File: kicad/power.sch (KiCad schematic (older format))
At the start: 12 parts, among them J4 UE27AC54100, U3 P-FET, U4 LM3671MF-3.3

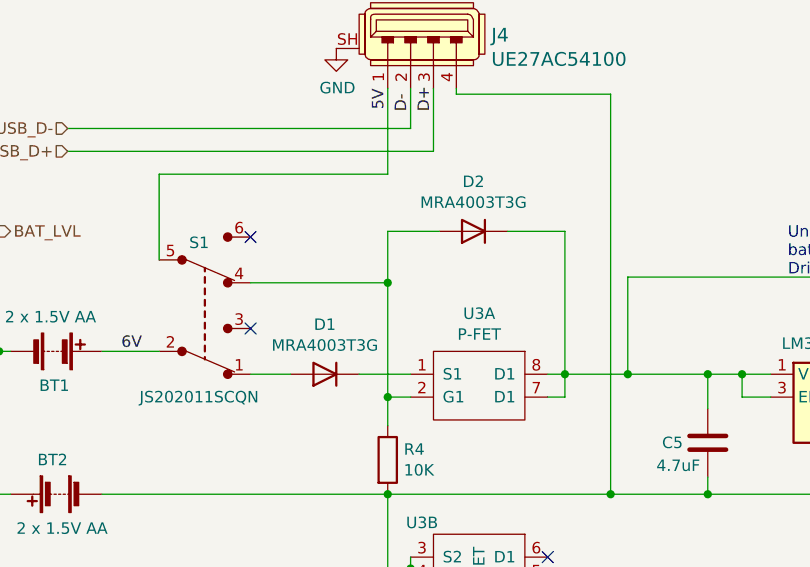
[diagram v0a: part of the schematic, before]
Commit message: Wired up buzzer and LDR
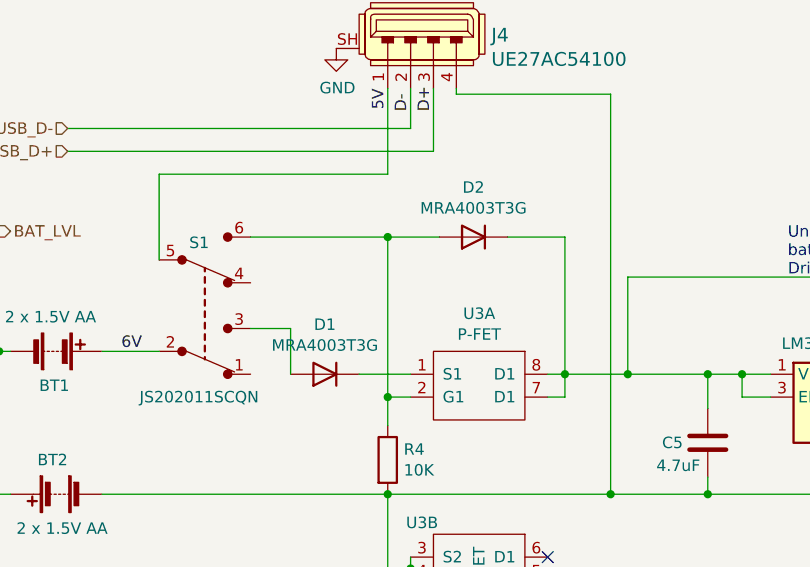
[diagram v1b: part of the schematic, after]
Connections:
- net at S1.1: no longer D1.2 (A)
- net at S1.3: now also D1.2 (A)
- net at D2.2 (A), R4.1, U3.2 (G1): now also S1.6; no longer S1.4
- no-connect marks 4 -> 2
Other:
- moved on the sheet: D2
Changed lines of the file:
@@
 	1    0    0    -1
 $EndComp
-Wire Wire Line
-	3625 3450 3400 3450
 $Comp
 L Device:R R4
@@
 Connection ~ 3525 3550
 Wire Wire Line
-	3750 2825 3525 2825
-Wire Wire Line
-	3525 2825 3525 3050
-Wire Wire Line
-	4050 2825 4300 2825
-Wire Wire Line
-	4300 2825 4300 3450
+	3750 2850 3525 2850
+Wire Wire Line
+	4050 2850 4300 2850
+Wire Wire Line
+	4300 2850 4300 3450
 Wire Wire Line
 	5075 3550 5075 3450
@@
 $EndComp
 Wire Wire Line
-	2925 3450 3100 3450
-Wire Wire Line
 	2275 3350 2525 3350
 Wire Wire Line
-	2925 3050 3525 3050
-Connection ~ 3525 3050
-Wire Wire Line
-	3525 3050 3525 3550
-Wire Wire Line
 	3525 2200 3525 2575
 Wire Wire Line
@@
 Wire Wire Line
 	2525 2575 2525 2950
-NoConn ~ 2925 2850
-NoConn ~ 2925 3250
 Wire Wire Line
 	4925 3975 5500 3975
@@
 	3525 4300 3525 3975
 $Comp
+L Diode:MRA4003T3G D2
+U 1 1 5FBAF34B
+P 3900 2850
+F 0 "D2" H 3900 2633 50  0000 C CNN
+F 1 "MRA4003T3G" H 3900 2724 50  0000 C CNN
+F 2 "Diode_SMD:D_SMA" H 3900 2675 50  0001 C CNN
+F 3 "http://www.onsemi.com/pub_link/Collateral/MRA4003T3-D.PDF" H 3900 2850 50  0001 C CNN
+	1    3900 2850
+	-1   0    0    1
+$EndComp
+Wire Wire Line
+	2925 2850 3525 2850
+Connection ~ 3525 2850
+Wire Wire Line
+	3525 2850 3525 3550
+Wire Wire Line
+	3625 3450 3400 3450
+$Comp
 L Diode:MRA4003T3G D1
 U 1 1 5FBA69DF
@@
 	-1   0    0    1
 $EndComp
-$Comp
-L Diode:MRA4003T3G D2
-U 1 1 5FBAF34B
-P 3900 2825
-F 0 "D2" H 3900 2608 50  0000 C CNN
-F 1 "MRA4003T3G" H 3900 2699 50  0000 C CNN
-F 2 "Diode_SMD:D_SMA" H 3900 2650 50  0001 C CNN
-F 3 "http://www.onsemi.com/pub_link/Collateral/MRA4003T3-D.PDF" H 3900 2825 50  0001 C CNN
-	1    3900 2825
-	-1   0    0    1
-$EndComp
+Wire Wire Line
+	3100 3450 3100 3250
+Wire Wire Line
+	3100 3250 2925 3250
 $EndSCHEMATC

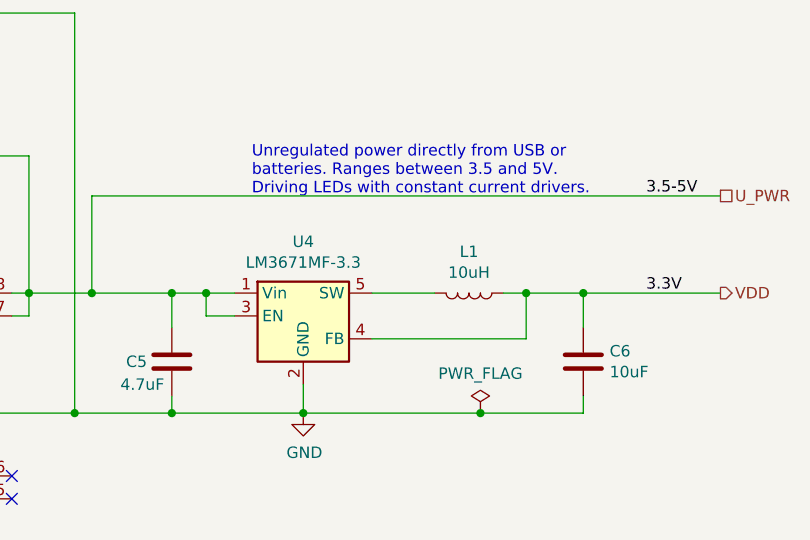
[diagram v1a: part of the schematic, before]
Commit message: Added power net and buck converter
Also wired up Ir transceiver.
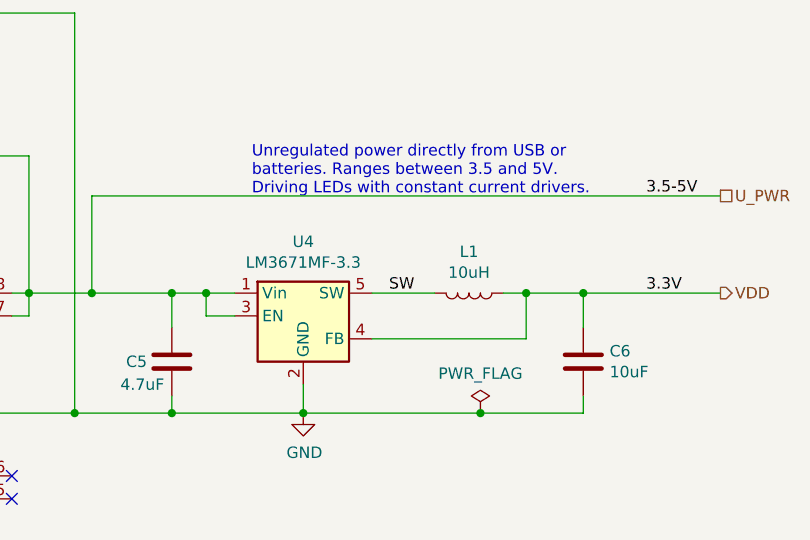
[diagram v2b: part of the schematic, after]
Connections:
- net SW: now reaches L1.2, U4.5 (SW)
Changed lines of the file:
@@
 Wire Wire Line
 	3100 3250 2925 3250
+Text Label 5875 3450 0    50   ~ 0
+SW
 $EndSCHEMATC

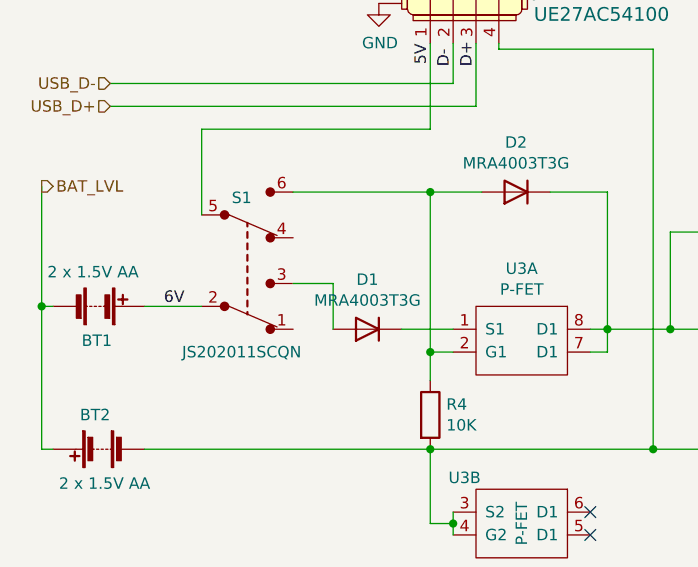
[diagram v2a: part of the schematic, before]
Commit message: Decouple microcontroller
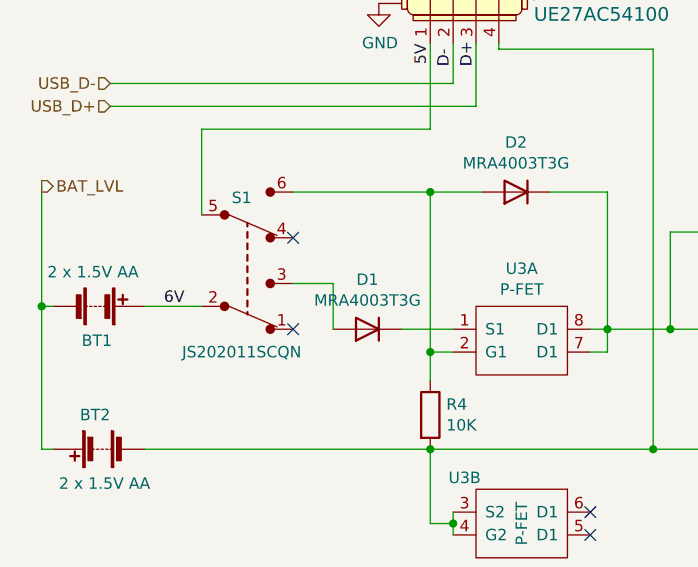
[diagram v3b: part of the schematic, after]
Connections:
- no-connect marks 2 -> 4
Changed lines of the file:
@@
 Text Label 5875 3450 0    50   ~ 0
 SW
+NoConn ~ 2925 3050
+NoConn ~ 2925 3450
 $EndSCHEMATC

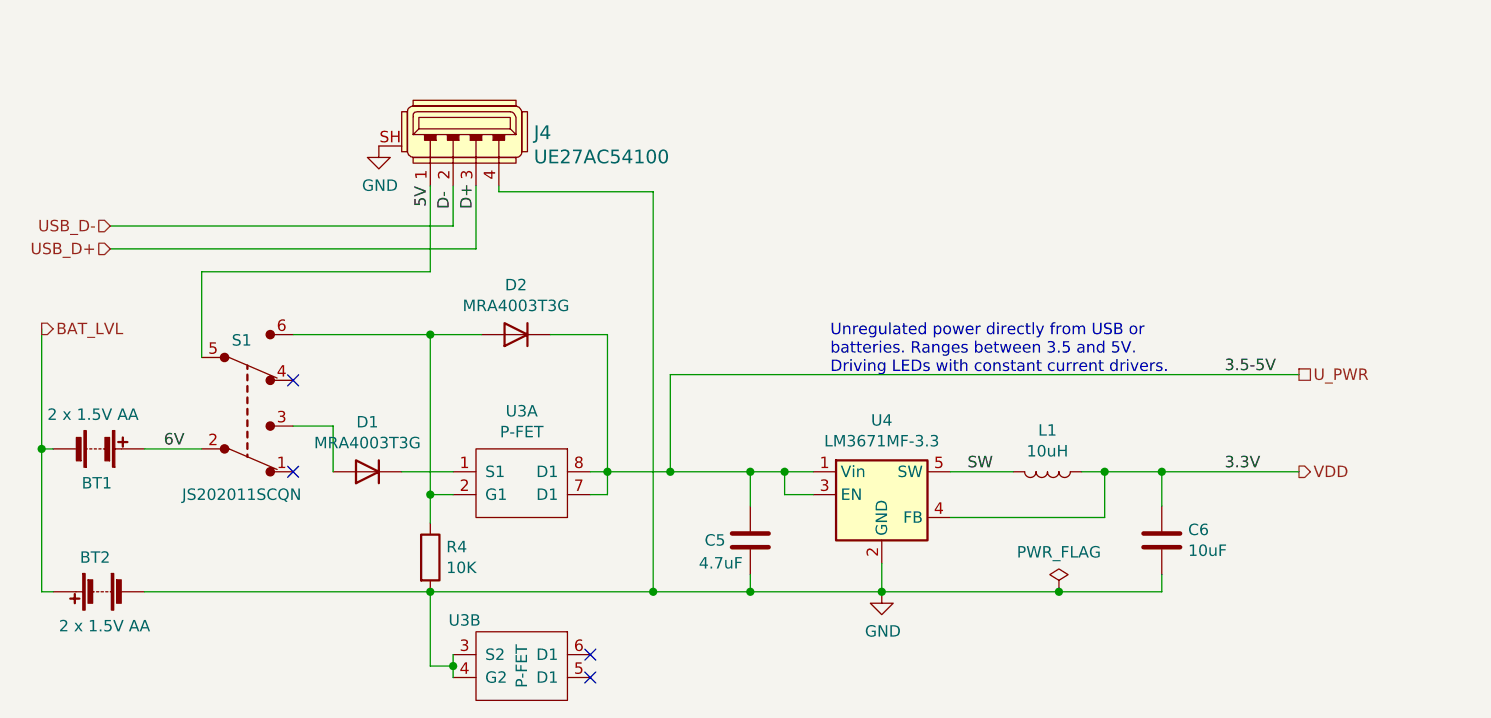
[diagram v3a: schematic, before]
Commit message: Adding level shifters
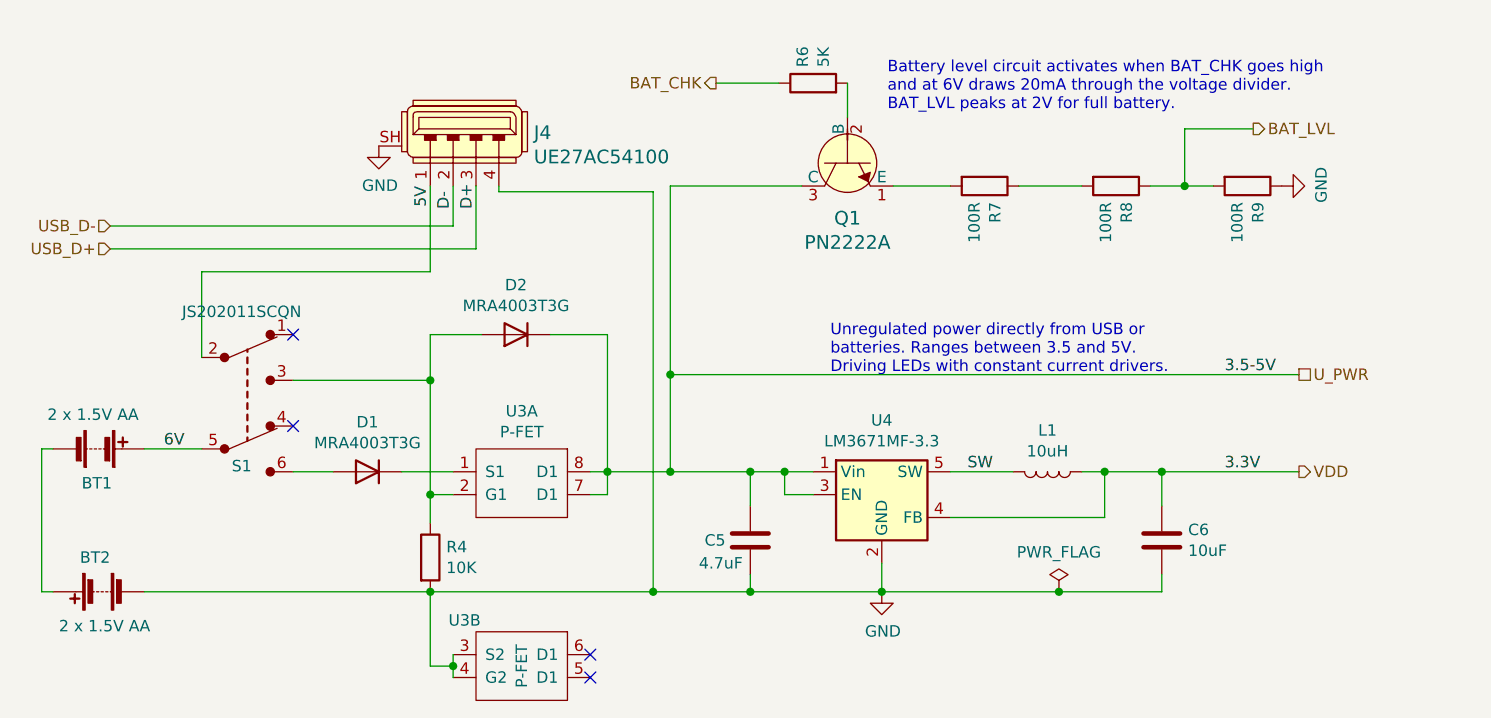
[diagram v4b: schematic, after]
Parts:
- added Q1: PN2222A, digikey-footprints:TO-92-3, symbol dk_Transistors-Bipolar-BJT-Single:PN2222A
- added R6: 5K, Resistor_SMD:R_0805_2012Metric_Pad1.15x1.40mm_HandSolder, symbol Device:R
- added R7, R8, R9: 100R, Resistor_SMD:R_0805_2012Metric_Pad1.15x1.40mm_HandSolder, symbol Device:R
- S1: footprint local:JS202011AQN_THT_DPDT -> Button_Switch_THT:SW_CuK_JS202011AQN_DPDT_Angled
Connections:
- net 5V: now also S1.2; no longer S1.5
- net 6V: now also S1.5; no longer S1.2
- net BAT_LVL: now also R8.1, R9.2; no longer BT1.2 (-), BT2.1 (+)
- net GND: now also R9.1
- net U_PWR: now also Q1.3 (C)
- net at S1.3: now also D2.2 (A), R4.1, U3.2 (G1); no longer D1.2 (A)
- new net: BT1.2 (-), BT2.1 (+)
- new net: D1.2 (A), S1.6
- new net: R7.1, R8.2
- new net: Q1.1 (E), R7.2
- new net: Q1.2 (B), R6.2
- new net BAT_CHK: R6.1
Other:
- note added: "Battery level circuit activates when BAT_CHK goes high\nand at 6V draws 20mA through the voltage divider.\nBAT_LVL peaks at 2V for full battery."
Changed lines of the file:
@@
 Wire Wire Line
 	4575 3450 4575 3025
-Wire Wire Line
-	4575 3025 7325 3025
 Connection ~ 4575 3450
 Wire Wire Line
@@
 Wire Wire Line
 	1875 3975 1825 3975
-Text HLabel 1825 2825 2    50   Output ~ 0
-BAT_LVL
 Wire Wire Line
 	1825 3975 1825 3350
 Connection ~ 3525 3975
-Wire Wire Line
-	1825 3350 1825 2825
-Connection ~ 1825 3350
 Text HLabel 7325 3025 2    50   UnSpc ~ 0
 U_PWR
@@
 Text HLabel 2125 2475 0    50   Input ~ 0
 USB_D+
+Wire Wire Line
+	2275 3350 2525 3350
+Wire Wire Line
+	3525 2200 3525 2575
+Wire Wire Line
+	3525 2575 2525 2575
+Wire Wire Line
+	4925 3975 5500 3975
+Wire Wire Line
+	5075 3550 5200 3550
+Wire Wire Line
+	4225 3550 4300 3550
+Wire Wire Line
+	4300 3550 4300 3450
+Wire Wire Line
+	3625 4350 3625 4300
+Wire Wire Line
+	3625 4300 3525 4300
+Connection ~ 3625 4300
+Wire Wire Line
+	3625 4300 3625 4250
+Wire Wire Line
+	3525 4300 3525 3975
+$Comp
+L Diode:MRA4003T3G D2
+U 1 1 5FBAF34B
+P 3900 2850
+F 0 "D2" H 3900 2633 50  0000 C CNN
+F 1 "MRA4003T3G" H 3900 2724 50  0000 C CNN
+F 2 "Diode_SMD:D_SMA" H 3900 2675 50  0001 C CNN
+F 3 "http://www.onsemi.com/pub_link/Collateral/MRA4003T3-D.PDF" H 3900 2850 50  0001 C CNN
+	1    3900 2850
+	-1   0    0    1
+$EndComp
+Wire Wire Line
+	3525 2850 3525 3050
+Wire Wire Line
+	3625 3450 3400 3450
+$Comp
+L Diode:MRA4003T3G D1
+U 1 1 5FBA69DF
+P 3250 3450
+F 0 "D1" H 3250 3233 50  0000 C CNN
+F 1 "MRA4003T3G" H 3250 3324 50  0000 C CNN
+F 2 "Diode_SMD:D_SMA" H 3250 3275 50  0001 C CNN
+F 3 "http://www.onsemi.com/pub_link/Collateral/MRA4003T3-D.PDF" H 3250 3450 50  0001 C CNN
+	1    3250 3450
+	-1   0    0    1
+$EndComp
+Text Label 5875 3450 0    50   ~ 0
+SW
+Text HLabel 7125 1950 2    50   Output ~ 0
+BAT_LVL
+Wire Wire Line
+	4575 3025 7325 3025
+NoConn ~ 4225 4250
+NoConn ~ 4225 4350
+$Comp
+L local:P-FET U?
+U 2 1 5F952E8F
+P 3925 4300
+AR Path="/6011206E/5F952E8F" Ref="U?"  Part="2"
+AR Path="/5F785555/5F952E8F" Ref="U3"  Part="2"
+F 0 "U3" H 3675 4500 50  0000 C CNN
+F 1 "P-FET" V 3925 4300 50  0000 C CNN
+F 2 "Package_SO:SOIC-8_3.9x4.9mm_P1.27mm" H 4125 4700 50  0001 C CNN
+F 3 "https://www.diodes.com/assets/Datasheets/DMP3085LSD.pdf" H 4125 4700 50  0001 C CNN
+	2    3925 4300
+	1    0    0    -1
+$EndComp
+$Comp
+L Device:R R7
+U 1 1 5FD60282
+P 5950 2200
+F 0 "R7" H 6020 2246 50  0000 L CNN
+F 1 "100R" H 6020 2155 50  0000 L CNN
+F 2 "Resistor_SMD:R_0805_2012Metric_Pad1.15x1.40mm_HandSolder" V 5880 2200 50  0001 C CNN
+F 3 "~" H 5950 2200 50  0001 C CNN
+	1    5950 2200
+	0    1    1    0
+$EndComp
+$Comp
+L Device:R R9
+U 1 1 5FD60513
+P 7100 2200
+F 0 "R9" H 7170 2246 50  0000 L CNN
+F 1 "100R" H 7170 2155 50  0000 L CNN
+F 2 "Resistor_SMD:R_0805_2012Metric_Pad1.15x1.40mm_HandSolder" V 7030 2200 50  0001 C CNN
+F 3 "~" H 7100 2200 50  0001 C CNN
+	1    7100 2200
+	0    1    1    0
+$EndComp
+$Comp
+L dk_Transistors-Bipolar-BJT-Single:PN2222A Q1
+U 1 1 5FD62F08
+P 5350 2100
+F 0 "Q1" V 5591 2100 60  0000 C CNN
+F 1 "PN2222A" V 5697 2100 60  0000 C CNN
+F 2 "digikey-footprints:TO-92-3" H 5550 2300 60  0001 L CNN
+F 3 "https://my.centralsemi.com/get_document.php?cmp=1&mergetype=pd&mergepath=pd&pdf_id=PN2221-2222A.PDF" H 5550 2400 60  0001 L CNN
+F 4 "PN2222ACS-ND" H 5550 2500 60  0001 L CNN "Digi-Key_PN"
+F 5 "PN2222A" H 5550 2600 60  0001 L CNN "MPN"
+F 6 "Discrete Semiconductor Products" H 5550 2700 60  0001 L CNN "Category"
+F 7 "Transistors - Bipolar (BJT) - Single" H 5550 2800 60  0001 L CNN "Family"
+F 8 "https://my.centralsemi.com/get_document.php?cmp=1&mergetype=pd&mergepath=pd&pdf_id=PN2221-2222A.PDF" H 5550 2900 60  0001 L CNN "DK_Datasheet_Link"
+F 9 "/product-detail/en/central-semiconductor-corp/PN2222A/PN2222ACS-ND/4806937" H 5550 3000 60  0001 L CNN "DK_Detail_Page"
+F 10 "TRANS NPN 40V 0.8A TO-92" H 5550 3100 60  0001 L CNN "Description"
+F 11 "Central Semiconductor Corp" H 5550 3200 60  0001 L CNN "Manufacturer"
+F 12 "Active" H 5550 3300 60  0001 L CNN "Status"
+	1    5350 2100
+	0    -1   1    0
+$EndComp
+Wire Wire Line
+	4575 3025 4575 2200
+Wire Wire Line
+	4575 2200 5150 2200
+Connection ~ 4575 3025
+Wire Wire Line
+	5550 2200 5800 2200
+Wire Wire Line
+	6950 2200 6825 2200
+$Comp
+L power:GND #PWR028
+U 1 1 5FD6BB5C
+P 7250 2200
+F 0 "#PWR028" H 7250 1950 50  0001 C CNN
+F 1 "GND" H 7255 2027 50  0000 C CNN
+F 2 "" H 7250 2200 50  0001 C CNN
+F 3 "" H 7250 2200 50  0001 C CNN
+	1    7250 2200
+	0    -1   -1   0
+$EndComp
+Text HLabel 4775 1750 0    50   Output ~ 0
+BAT_CHK
+Wire Wire Line
+	4775 1750 5050 1750
+Wire Wire Line
+	5350 1750 5350 1900
+Connection ~ 6825 2200
+Wire Wire Line
+	6825 2200 6675 2200
+$Comp
+L Device:R R8
+U 1 1 5FD71537
+P 6525 2200
+F 0 "R8" H 6595 2246 50  0000 L CNN
+F 1 "100R" H 6595 2155 50  0000 L CNN
+F 2 "Resistor_SMD:R_0805_2012Metric_Pad1.15x1.40mm_HandSolder" V 6455 2200 50  0001 C CNN
+F 3 "~" H 6525 2200 50  0001 C CNN
+	1    6525 2200
+	0    1    1    0
+$EndComp
+Wire Wire Line
+	6375 2200 6100 2200
+$Comp
+L Device:R R6
+U 1 1 5FD7FD32
+P 5200 1750
+F 0 "R6" H 5270 1796 50  0000 L CNN
+F 1 "5K" H 5270 1705 50  0000 L CNN
+F 2 "Resistor_SMD:R_0805_2012Metric_Pad1.15x1.40mm_HandSolder" V 5130 1750 50  0001 C CNN
+F 3 "~" H 5200 1750 50  0001 C CNN
+	1    5200 1750
+	0    -1   -1   0
+$EndComp
+Text Notes 5525 1875 0    50   ~ 0
+Battery level circuit activates when BAT_CHK goes high\nand at 6V draws 20mA through the voltage divider.\nBAT_LVL peaks at 2V for full battery.
+Wire Wire Line
+	6825 1950 7125 1950
+Wire Wire Line
+	6825 1950 6825 2200
+Wire Wire Line
+	2525 2575 2525 2950
 $Comp
 L dk_Slide-Switches:JS202011SCQN S1
@@
 F 0 "S1" H 2700 2875 50  0000 C CNN
 F 1 "JS202011SCQN" H 2700 3550 50  0000 C CNN
-F 2 "local:JS202011AQN_THT_DPDT" H 2925 3350 50  0001 L CNN
+F 2 "Button_Switch_THT:SW_CuK_JS202011AQN_DPDT_Angled" H 2925 3350 50  0001 L CNN
 F 3 "https://www.ckswitches.com/media/1422/js.pdf" H 2925 3450 60  0001 L CNN
 F 4 "401-2002-1-ND" H 2925 3550 60  0001 L CNN "Digi-Key_PN"
@@
 F 12 "Active" H 2925 4350 60  0001 L CNN "Status"
 	1    2725 3150
-	1    0    0    1
-$EndComp
-Wire Wire Line
-	2275 3350 2525 3350
-Wire Wire Line
-	3525 2200 3525 2575
-Wire Wire Line
-	3525 2575 2525 2575
-Wire Wire Line
-	2525 2575 2525 2950
-Wire Wire Line
-	4925 3975 5500 3975
-Wire Wire Line
-	5075 3550 5200 3550
-Wire Wire Line
-	4225 3550 4300 3550
-Wire Wire Line
-	4300 3550 4300 3450
-$Comp
-L local:P-FET U?
-U 2 1 5F952E8F
-P 3925 4300
-AR Path="/6011206E/5F952E8F" Ref="U?"  Part="2"
-AR Path="/5F785555/5F952E8F" Ref="U3"  Part="2"
-F 0 "U3" H 3675 4500 50  0000 C CNN
-F 1 "P-FET" V 3925 4300 50  0000 C CNN
-F 2 "Package_SO:SOIC-8_3.9x4.9mm_P1.27mm" H 4125 4700 50  0001 C CNN
-F 3 "https://www.diodes.com/assets/Datasheets/DMP3085LSD.pdf" H 4125 4700 50  0001 C CNN
-	2    3925 4300
 	1    0    0    -1
 $EndComp
-NoConn ~ 4225 4350
-NoConn ~ 4225 4250
-Wire Wire Line
-	3625 4350 3625 4300
-Wire Wire Line
-	3625 4300 3525 4300
-Connection ~ 3625 4300
-Wire Wire Line
-	3625 4300 3625 4250
-Wire Wire Line
-	3525 4300 3525 3975
-$Comp
-L Diode:MRA4003T3G D2
-U 1 1 5FBAF34B
-P 3900 2850
-F 0 "D2" H 3900 2633 50  0000 C CNN
-F 1 "MRA4003T3G" H 3900 2724 50  0000 C CNN
-F 2 "Diode_SMD:D_SMA" H 3900 2675 50  0001 C CNN
-F 3 "http://www.onsemi.com/pub_link/Collateral/MRA4003T3-D.PDF" H 3900 2850 50  0001 C CNN
-	1    3900 2850
-	-1   0    0    1
-$EndComp
-Wire Wire Line
-	2925 2850 3525 2850
-Connection ~ 3525 2850
-Wire Wire Line
-	3525 2850 3525 3550
-Wire Wire Line
-	3625 3450 3400 3450
-$Comp
-L Diode:MRA4003T3G D1
-U 1 1 5FBA69DF
-P 3250 3450
-F 0 "D1" H 3250 3233 50  0000 C CNN
-F 1 "MRA4003T3G" H 3250 3324 50  0000 C CNN
-F 2 "Diode_SMD:D_SMA" H 3250 3275 50  0001 C CNN
-F 3 "http://www.onsemi.com/pub_link/Collateral/MRA4003T3-D.PDF" H 3250 3450 50  0001 C CNN
-	1    3250 3450
-	-1   0    0    1
-$EndComp
-Wire Wire Line
-	3100 3450 3100 3250
-Wire Wire Line
-	3100 3250 2925 3250
-Text Label 5875 3450 0    50   ~ 0
-SW
-NoConn ~ 2925 3050
-NoConn ~ 2925 3450
+Wire Wire Line
+	3100 3450 2925 3450
+Wire Wire Line
+	2925 3050 3525 3050
+Connection ~ 3525 3050
+Wire Wire Line
+	3525 3050 3525 3550
+NoConn ~ 2925 2850
+NoConn ~ 2925 3250
 $EndSCHEMATC
